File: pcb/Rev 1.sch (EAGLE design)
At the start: 248 parts, among them J1 3220-10-0100-00, J2 10118194-0001LF, J3 B2B-PH-K-S(LF)(SN), Q1 MMBT3904,215MMBT3904,215, Q10 MMBT3904,215MMBT3904,215, Q11 MMBT3904,215MMBT3904,215, Q12 MMBT3904,215MMBT3904,215, Q13 MMBT3904,215MMBT3904,215, Q14 MMBT3904,215MMBT3904,215, Q15 MMBT3904,215MMBT3904,215, Q16 TEFT4300, Q17 TEFT4300, Q18 TEFT4300, Q19 TEFT4300, Q2 MMBT3904,215MMBT3904,215, Q20 MMBT3904,215MMBT3904,215, Q21 MMBT3904,215MMBT3904,215, Q22 MMBT3904,215MMBT3904,215, Q23 MMBT3904,215MMBT3904,215, Q24 TEFT4300, Q25 TEFT4300, Q26 TEFT4300, Q27 TEFT4300, Q28 SI7157DP, Q29 SI7157DP, Q3 MMBT3904,215MMBT3904,215, Q30 MMBT3906, Q31 MMBT3906, Q32 SI7157DP, Q33 MMBT3906, Q34 MMBT3906, Q4 MMBT3904,215MMBT3904,215, Q5 MMBT3904,215MMBT3904,215, Q6 MMBT3904,215MMBT3904,215, Q7 MMBT3904,215MMBT3904,215, Q8 MMBT3904,215MMBT3904,215, Q9 MMBT3904,215MMBT3904,215, SW1 210-6MS, U1 ATSAMD21G18A-MU, U10 DRV8871, U2 AP3441, U3 TPS61089, U4 BNO055, U5 MCP73811, U7 DRV8871, U8 DRV8871, U9 DRV8871

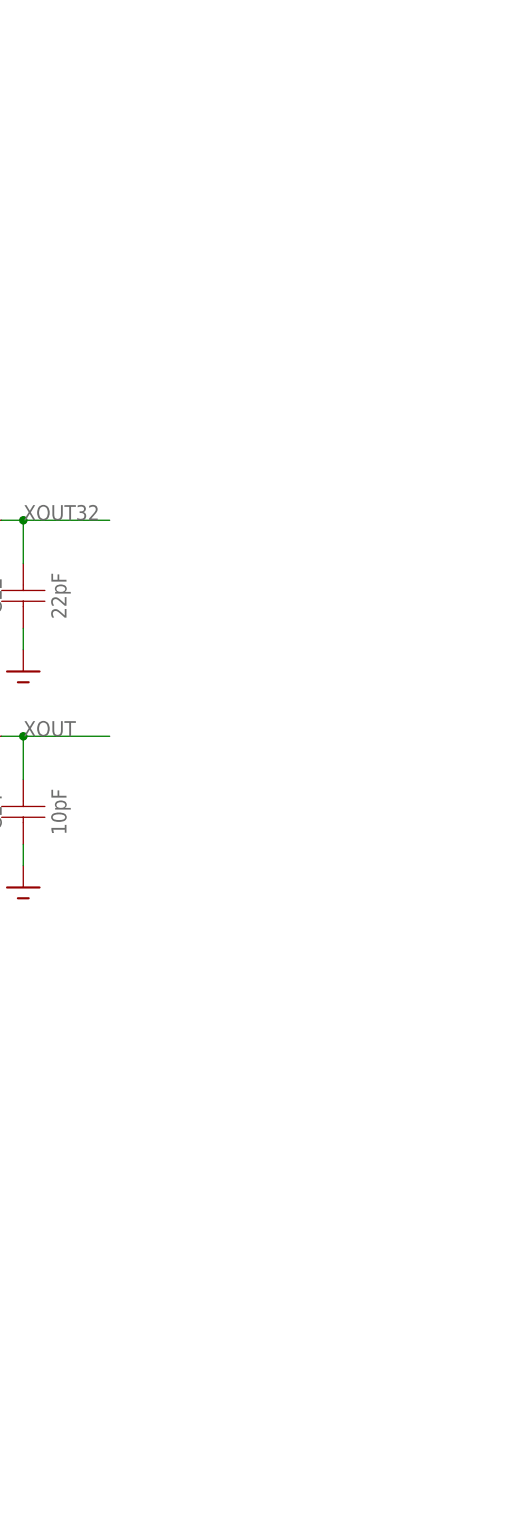
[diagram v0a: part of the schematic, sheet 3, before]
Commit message: Added note about pin mappings
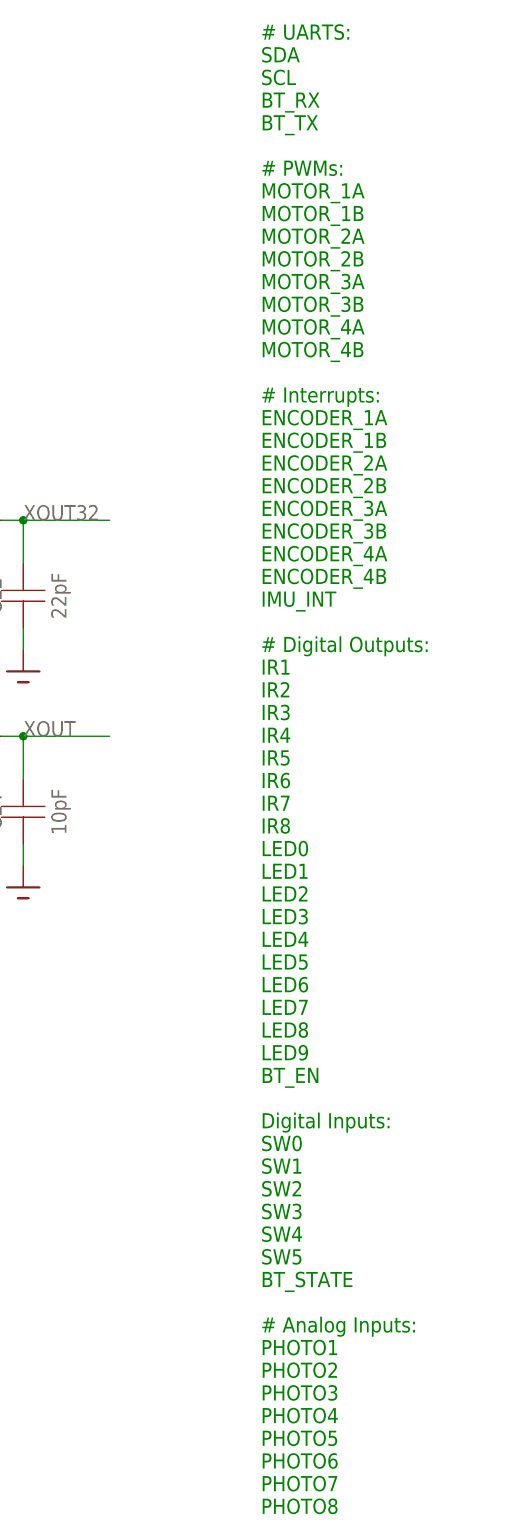
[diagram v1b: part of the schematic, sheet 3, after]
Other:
- note added: "# UARTS: SDA SCL BT_RX BT_TX # PWMs: MOTOR_1A MOTOR_1B MOTOR_2A MOTOR_2B MOTOR_3A MOTOR_3B MOTOR_4A MOTOR_4B # Interrupts: ENCODER_1A ENCODER_1B ENCODER_2A ENCODER_2B ENCODER_3A ENCODER_3B ENCODER_4A ENCODER_4B IMU_INT # Digital Outputs: IR1 IR2 IR3 IR4 IR5 IR6 IR7 IR8 LED0 LED1 LED2 LED3 LED4 LED5 LED6 LED7 LED8 LED9 BT_EN Digital Inputs: SW0 SW1 SW2 SW3 SW4 SW5 BT_STATE # Analog Inputs: PHOTO1 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"
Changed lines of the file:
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@@
 <description>MCU</description>
 <plain>
+<text x="215.9" y="-60.96" size="1.778" layer="91"># UARTS:
+SDA
+SCL
+BT_RX
+BT_TX
+# PWMs:
+MOTOR_1A
+MOTOR_1B
+MOTOR_2A
+MOTOR_2B
+MOTOR_3A
+MOTOR_3B
+MOTOR_4A
+MOTOR_4B
+# Interrupts:
+ENCODER_1A
+ENCODER_1B
+ENCODER_2A
+ENCODER_2B
+ENCODER_3A
+ENCODER_3B
+ENCODER_4A
+ENCODER_4B
+IMU_INT
+# Digital Outputs:
+IR1
+IR2
+IR3
+IR4
+IR5
+IR6
+IR7
+IR8
+LED0
+LED1
+LED2
+LED3
+LED4
+LED5
+LED6
+LED7
+LED8
+LED9
+BT_EN
+Digital Inputs:
+SW0
+SW1
+SW2
+SW3
+SW4
+SW5
+BT_STATE
+# Analog Inputs:
+PHOTO1
+PHOTO2
+PHOTO3
+PHOTO4
+PHOTO5
+PHOTO6
+PHOTO7
+PHOTO8</text>
 </plain>
 <instances>
@@
 </drawing>
 <compatibility>
+<note version="6.3" minversion="6.2.2" severity="warning">
+Since Version 6.2.2 text objects can contain more than one line,
+which will not be processed correctly with this version.
+</note>
 <note version="8.3" severity="warning">
 Since Version 8.3, EAGLE supports URNs for individual library

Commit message: Removed the DIP switches and some LEDs
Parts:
- removed C47, C48, C49, C50, C51: 1uF, Micromouse 2020:CAPACITOR0603
- removed C77: 0.1uF, Micromouse 2020:CAPACITOR0603
- removed D10, D11, D7, D8, D9: LED1206, Micromouse 2020:LED1206
- removed Q10, Q11, Q7, Q8, Q9: MMBT3904,215MMBT3904,215, Micromouse 2020:MMBT3904,215MMBT3904,215
- removed R21, R22, R23, R24, R25: 30R, Micromouse 2020:RESISTOR0603
- removed R71, R72, R73, R74, R75, R76: 10k, Micromouse 2020:RESISTOR0603
- removed R81, R82, R83, R84, R85, R86: 470k, Micromouse 2020:RESISTOR0603
- removed SW1: 210-6MS, Micromouse 2020:210-6MS
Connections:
- removed net LED5: Q7.B
- removed net LED6: Q8.B
- removed net LED7: Q9.B
- removed net LED8: Q10.B
- removed net LED9: Q11.B
- removed net N$100: R73.P$2, SW1.4B
- removed net N$101: R74.P$2, SW1.3B
- removed net N$102: R75.P$2, SW1.2B
- removed net N$103: R76.P$2, SW1.1B
- removed net N$30: Q7.C, R21.P$1
- removed net N$31: Q8.C, R22.P$1
- removed net N$32: Q9.C, R23.P$1
- removed net N$33: Q10.C, R24.P$1
- removed net N$34: Q11.C, R25.P$1
- removed net N$35: D7.OUT, R21.P$2
- removed net N$36: D8.OUT, R22.P$2
- removed net N$37: D9.OUT, R23.P$2
- removed net N$38: D10.OUT, R24.P$2
- removed net N$39: D11.OUT, R25.P$2
- removed net N$98: R71.P$2, SW1.6B
- removed net N$99: R72.P$2, SW1.5B
- removed net SW0: R86.P$1, SW1.1A
- removed net SW1: R85.P$1, SW1.2A
- removed net SW2: R84.P$1, SW1.3A
- removed net SW3: R83.P$1, SW1.4A
- removed net SW4: R82.P$1, SW1.5A
- removed net SW5: R81.P$1, SW1.6A
- net +3V3: no longer C47.P$2, C48.P$2, C49.P$2, C50.P$2, C51.P$2, C77.P$2, D10.IN, D11.IN, D7.IN, D8.IN, D9.IN, R81.P$2, R82.P$2, R83.P$2, R84.P$2, R85.P$2, R86.P$2
- net GND: no longer C47.P$1, C48.P$1, C49.P$1, C50.P$1, C51.P$1, C77.P$1, Q10.E, Q11.E, Q7.E, Q8.E, Q9.E, R71.P$1, R72.P$1, R73.P$1, R74.P$1, R75.P$1, R76.P$1
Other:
- note added: "# UARTS: SDA SCL BT_RX BT_TX # PWMs: MOTOR_1A MOTOR_1B MOTOR_2A MOTOR_2B MOTOR_3A MOTOR_3B MOTOR_4A MOTOR_4B # Interrupts: ENCODER_1A ENCODER_1B ENCODER_2A ENCODER_2B ENCODER_3A ENCODER_3B ENCODER_4A ENCODER_4B IMU_INT # Digital Outputs: IR1 IR2 IR3 IR4 IR5 IR6 IR7 IR8 LED0 LED1 LED2 LED3 LED4 BT_EN Digital Inputs: BT_STATE # Analog Inputs: PHOTO1 PHOTO2 PHOTO3 PHOTO4 PHOTO5 PHOTO6 PHOTO7 PHOTO8"
- note removed: "# UARTS: SDA SCL BT_RX BT_TX # PWMs: MOTOR_1A MOTOR_1B MOTOR_2A MOTOR_2B MOTOR_3A MOTOR_3B MOTOR_4A MOTOR_4B # Interrupts: ENCODER_1A ENCODER_1B ENCODER_2A ENCODER_2B ENCODER_3A ENCODER_3B ENCODER_4A ENCODER_4B IMU_INT # Digital Outputs: IR1 IR2 IR3 IR4 IR5 IR6 IR7 IR8 LED0 LED1 LED2 LED3 LED4 LED5 LED6 LED7 LED8 LED9 BT_EN Digital Inputs: SW0 SW1 SW2 SW3 SW4 SW5 BT_STATE # Analog Inputs: PHOTO1 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"

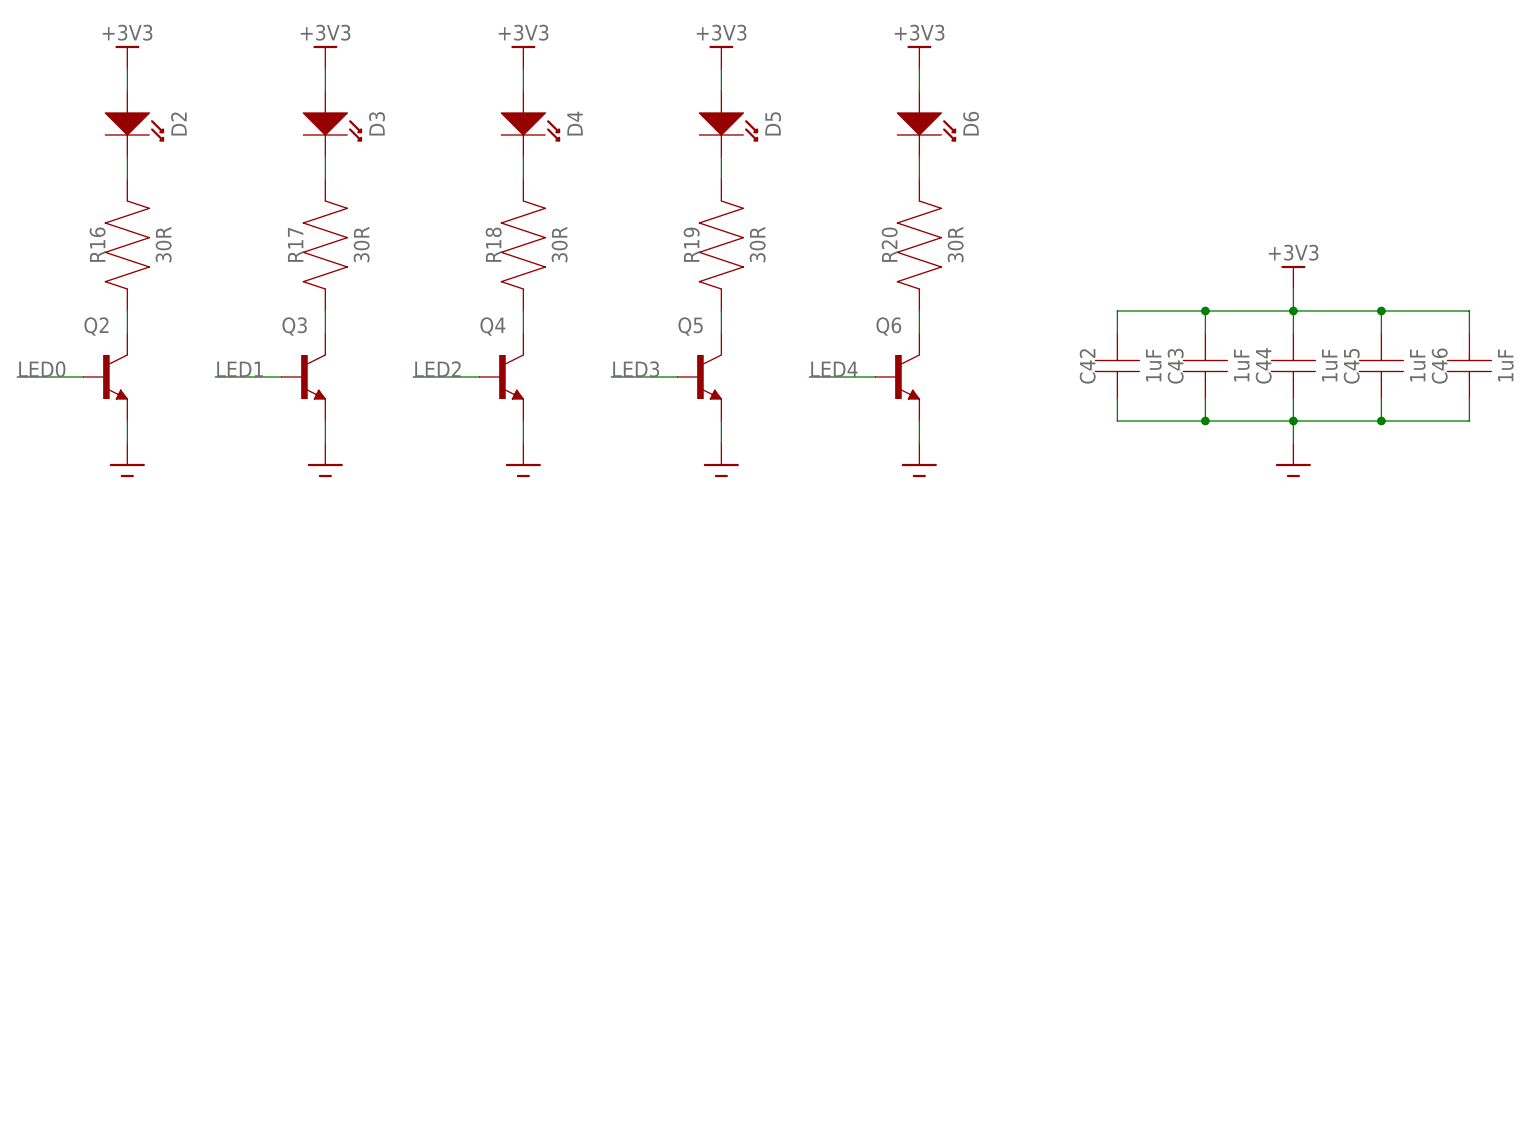
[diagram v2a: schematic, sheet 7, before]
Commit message: Added IO expanders
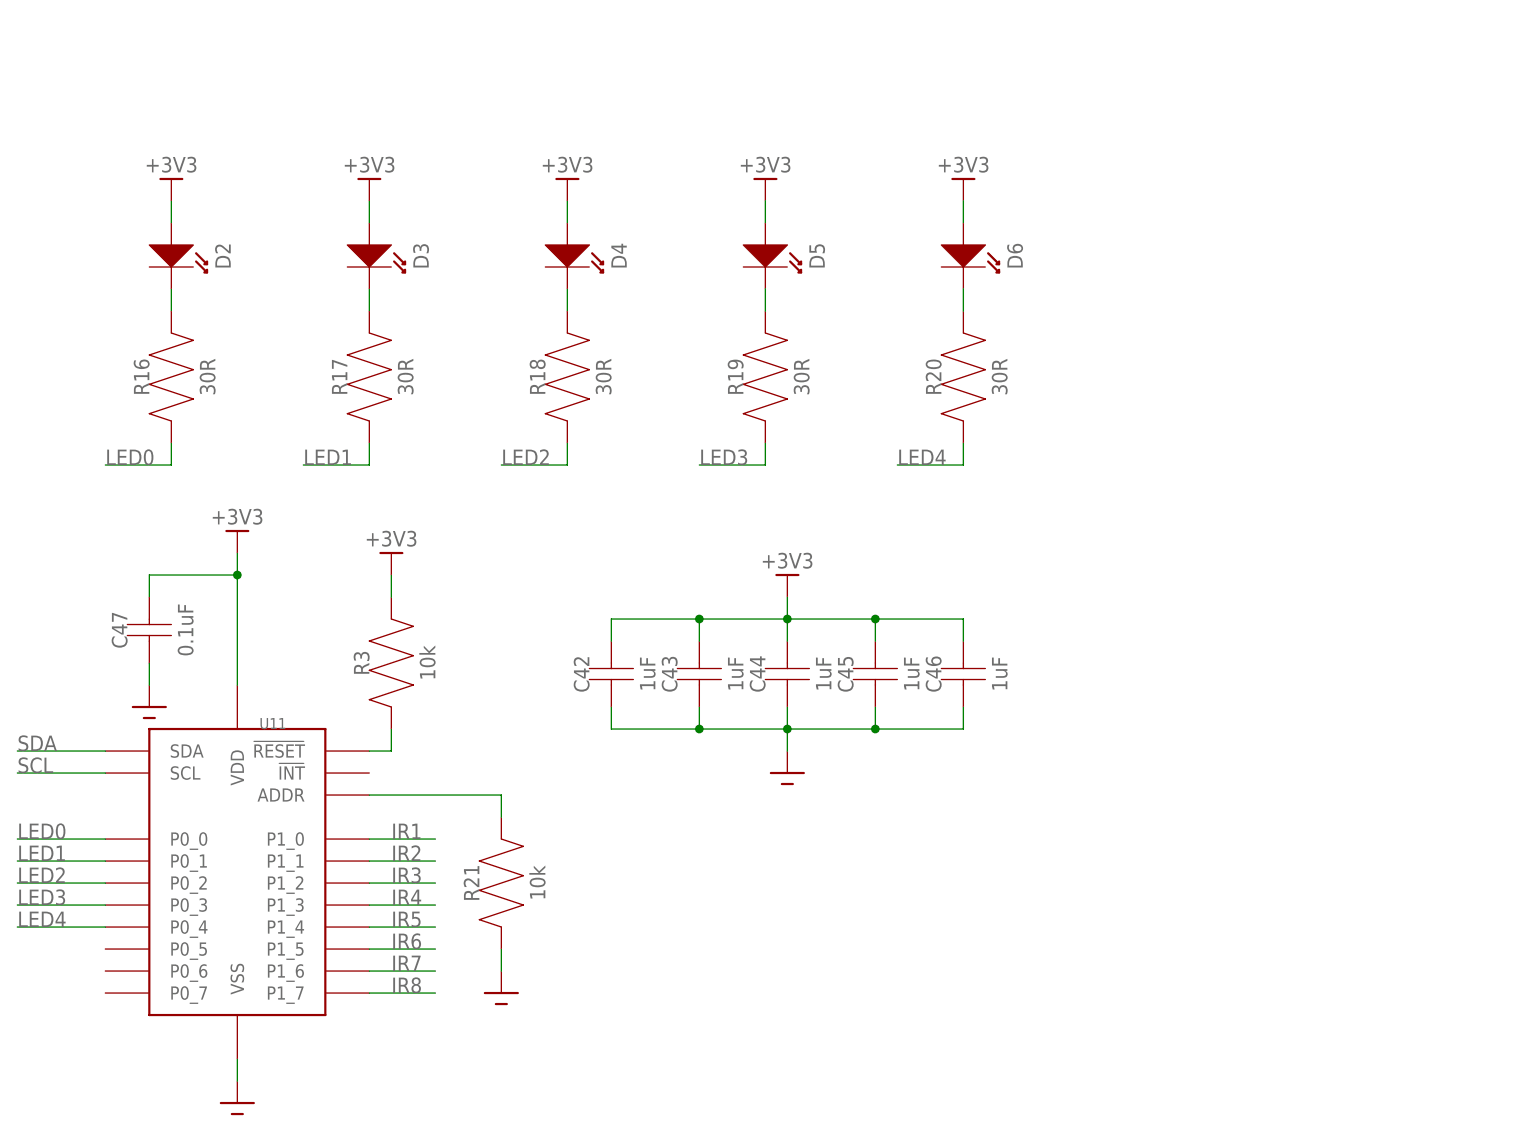
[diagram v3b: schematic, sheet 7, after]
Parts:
- removed Q2, Q3, Q4, Q5, Q6: MMBT3904,215MMBT3904,215, Micromouse 2020:MMBT3904,215MMBT3904,215
- added C47, C48: 0.1uF, Micromouse 2020:CAPACITOR0603
- added R21, R22, R23, R24, R3: 10k, Micromouse 2020:RESISTOR0603
- added U11: PCAL6416A, Micromouse 2020:PCAL6416A
- added U12: MAX7315, Micromouse 2020:MAX7315
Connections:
- removed net N$20: Q2.C, R16.P$1
- removed net N$24: Q6.C, R20.P$1
- new net N$31: R3.P$1, U11.!RESET
- new net N$32: R21.P$2, U11.ADDR
- net +3V3: now also C47.P$2, C48.P$2, R3.P$2, U11.VDD, U12.V+
- net GND: now also C47.P$1, C48.P$1, R21.P$1, R22.P$1, R23.P$1, R24.P$1, U11.VSS, U12.GND; no longer Q2.E, Q3.E, Q4.E, Q5.E, Q6.E
- net IR1: now also U11.P1_0
- net IR2: now also U11.P1_1
- net IR3: now also U11.P1_2
- net IR4: now also U11.P1_3
- net IR5: now also U11.P1_4
- net IR6: now also U11.P1_5
- net IR7: now also U11.P1_6
- net IR8: now also U11.P1_7
- net LED0: now also R16.P$1, U11.P0_0; no longer Q2.B
- net LED1: now also R17.P$1, U11.P0_1; no longer Q3.B
- net LED2: now also R18.P$1, U11.P0_2; no longer Q4.B
- net LED3: now also R19.P$1, U11.P0_3; no longer Q5.B
- net LED4: now also R20.P$1, U11.P0_4; no longer Q6.B
- net MOTOR_1A: now also U12.P1
- net MOTOR_1B: now also U12.P2
- net MOTOR_2A: now also U12.P3
- net MOTOR_2B: now also U12.P4
- net MOTOR_3A: now also U12.P5
- net MOTOR_3B: now also U12.P6
- net MOTOR_4A: now also U12.P7
- net MOTOR_4B: now also U12.P8
- net N$21: now also R22.P$2, U12.AD2; no longer Q3.C, R17.P$1
- net N$22: now also R23.P$2, U12.AD1; no longer Q4.C, R18.P$1
- net N$23: now also R24.P$2, U12.AD0; no longer Q5.C, R19.P$1
- net SCL: now also U11.SCL, U12.SCL
- net SDA: now also U11.SDA, U12.SDA
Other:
- note added: "# UARTS: SDA SCL BT_RX BT_TX # Interrupts: ENCODER_1A ENCODER_1B ENCODER_2A ENCODER_2B ENCODER_3A ENCODER_3B ENCODER_4A ENCODER_4B IMU_INT # Digital Outputs: BT_EN Digital Inputs: BT_STATE # Analog Inputs: PHOTO1 PHOTO2 PHOTO3 PHOTO4 PHOTO5 PHOTO6 PHOTO7 PHOTO8"
- note removed: "# UARTS: SDA SCL BT_RX BT_TX # PWMs: MOTOR_1A MOTOR_1B MOTOR_2A MOTOR_2B MOTOR_3A MOTOR_3B MOTOR_4A MOTOR_4B # Interrupts: ENCODER_1A ENCODER_1B ENCODER_2A ENCODER_2B ENCODER_3A ENCODER_3B ENCODER_4A ENCODER_4B IMU_INT # Digital Outputs: IR1 IR2 IR3 IR4 IR5 IR6 IR7 IR8 LED0 LED1 LED2 LED3 LED4 BT_EN Digital Inputs: BT_STATE # Analog Inputs: PHOTO1 PHOTO2 PHOTO3 PHOTO4 PHOTO5 PHOTO6 PHOTO7 PHOTO8"
- moved on the sheet: C42, C43, C44, C45, C46, D2, D3, D4, D5, D6, R16, R17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
